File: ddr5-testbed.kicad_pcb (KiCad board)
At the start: 6 copper layers, 69.6 x 30 mm, 67 parts, among them IC1 PCA6408APW, IC2 AT24CS01, J1 ddr4-sodimm-edge-connector, U1 MT60B2G8HB-48B_A, U2 TPS613221ADBVT

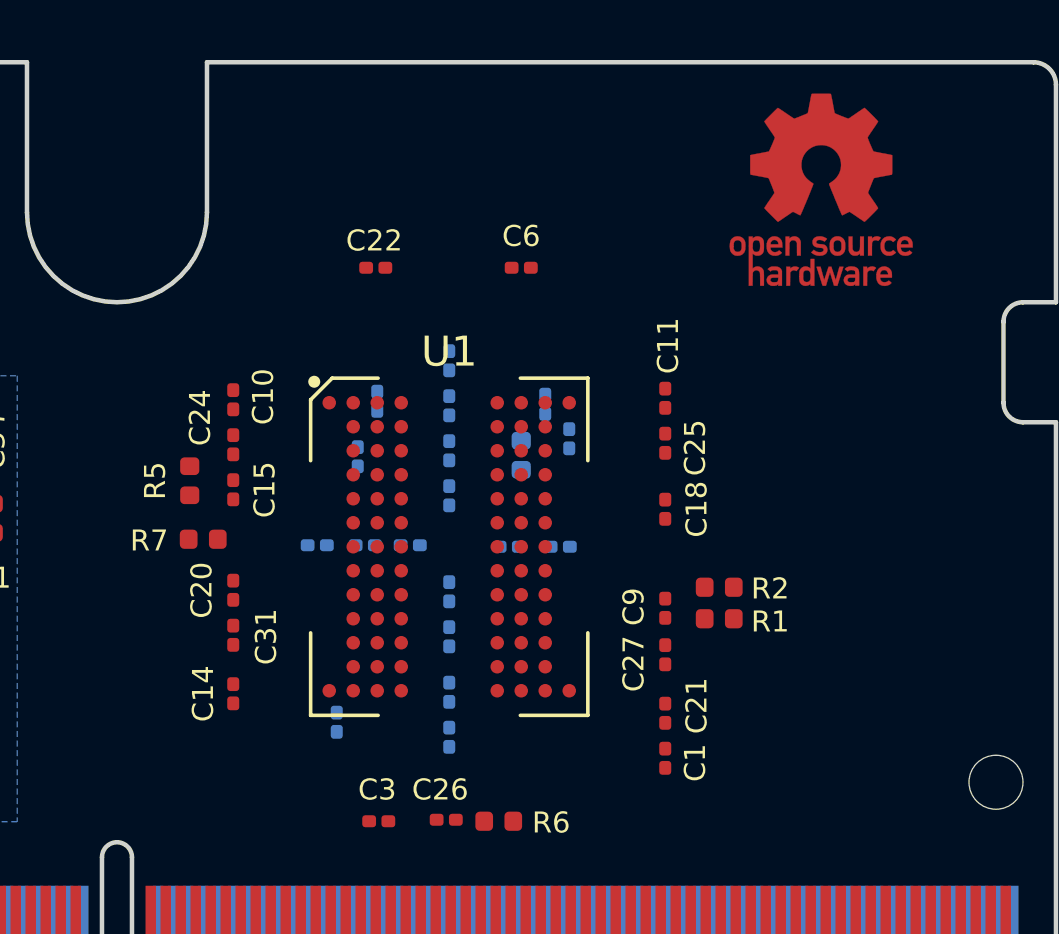
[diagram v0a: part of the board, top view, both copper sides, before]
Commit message: Fix power labels naming scheme, remove connection from SODIM to VDDQ, add chockes to DDR5 power
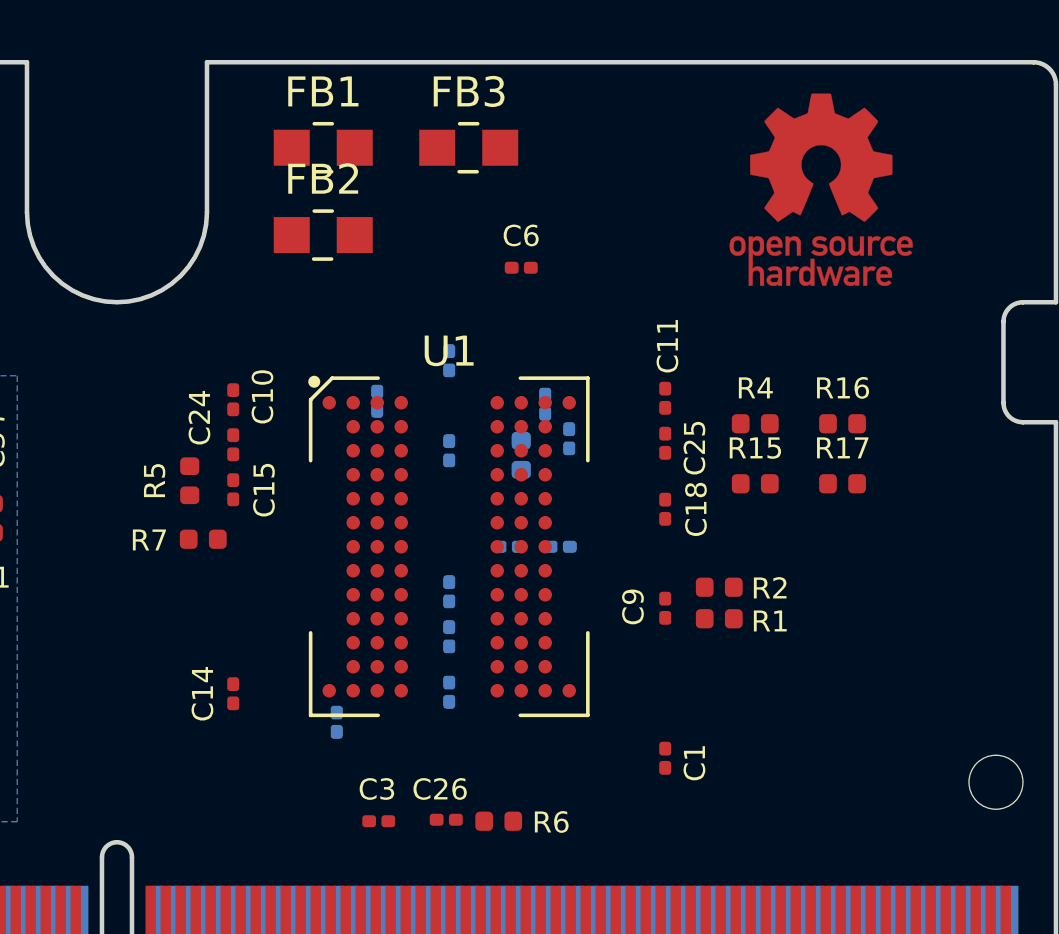
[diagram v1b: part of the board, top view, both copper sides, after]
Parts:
- removed C16, C17, C19, C20, C21, C22, C27, C29, C31, C33, C35, C36: C_100n_0201, ddr5-testbed-footprints:0201-res
- added FB1: 742792022, ddr5-testbed-footprints:0805-res, F.Cu at (145.2, 72.8)
- added FB2: 742792022, ddr5-testbed-footprints:0805-res, F.Cu at (145.2, 75.8)
- added FB3: 742792022, ddr5-testbed-footprints:0805-res, F.Cu at (150.0, 72.8)
- added R15: R_0R_0402, ddr5-testbed-footprints:0402-res, F.Cu at (159.6, 84.0)
- added R16: R_0R_0402, ddr5-testbed-footprints:0402-res, F.Cu at (162.5, 82.0)
- added R17: R_0R_0402, ddr5-testbed-footprints:0402-res, F.Cu at (162.5, 84.0)
- added R4: R_0R_0402, ddr5-testbed-footprints:0402-res, F.Cu at (159.6, 82.0)
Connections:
- net VDDLED renamed /EEPROM/VDD_LED
- C12 pad 1: VDD2 -> VDD
- C15 pad 1: VDD2 -> VDD
- C18 pad 1: VDD2 -> VDDQ
- C23 pad 1: VDD2 -> VDD
- C24 pad 1: VDD1 -> VPP
- C25 pad 1: VDD1 -> VPP
- C26 pad 1: VDD2 -> VDD
- C28 pad 1: VDD2 -> VDD
- C3 pad 1: VDD2 -> VDD
- C30 pad 1: VDD2 -> VDD
- C32 pad 1: VDD2 -> VDD
- C34 pad 1: VDD1 -> 1V8_SYS
- C38 pad 1: VDD1 -> 1V8_SYS
- C39 pad 1: VDD1 -> 1V8_SYS
- C6 pad 1: VDD2 -> VDD
- C9 pad 1: VDD2 -> VDD
- IC1 pad 1: VDD1 -> 1V8_SYS
- IC1 pad 2: VDD1 -> 1V8_SYS
- IC1 pad 3: VDD1 -> 1V8_SYS
- IC2 pad 4: VDD1 -> 1V8_SYS
- J1 pad 101: VDD2 -> 1V1_SYS
- J1 pad 103: VDD2 -> 1V1_SYS
- J1 pad 105: VDD2 -> 1V1_SYS
- J1 pad 107: VDD2 -> 1V1_SYS
- J1 pad 116: VDD1 -> 1V8_SYS
- J1 pad 118: VDD1 -> 1V8_SYS
- J1 pad 120: VDD1 -> 1V8_SYS
- J1 pad 122: VDD1 -> 1V8_SYS
- J1 pad 124: VDD1 -> 1V8_SYS
- J1 pad 126: VDDQ -> (no net)
- J1 pad 128: VDDQ -> (no net)
- J1 pad 130: VDDQ -> (no net)
- J1 pad 156: (no net) -> CA5
- J1 pad 158: (no net) -> CA4
- J1 pad 160: (no net) -> CA3
- J1 pad 162: (no net) -> CA2
- J1 pad 163: (no net) -> CA9
- J1 pad 164: (no net) -> CLK_N
- J1 pad 165: (no net) -> CA8
- J1 pad 166: (no net) -> CLK_P
- J1 pad 167: (no net) -> CA7
- J1 pad 169: (no net) -> CA6
- J1 pad 171: (no net) -> MIR
- J1 pad 172: (no net) -> ALERT_N
- J1 pad 173: (no net) -> TDQS_N
- J1 pad 174: (no net) -> LBDQ
- J1 pad 175: (no net) -> TDQS_P
- J1 pad 176: (no net) -> LBDQS
- J1 pad 179: (no net) -> CA13
- J1 pad 181: (no net) -> CA12
- J1 pad 183: (no net) -> CA11
- J1 pad 185: (no net) -> CA10
- J1 pad 187: (no net) -> DQ4
- J1 pad 189: (no net) -> DQ5
- J1 pad 191: (no net) -> DQ6
- J1 pad 193: (no net) -> DQ7
- J1 pad 194: (no net) -> CS_N
- J1 pad 196: (no net) -> TEN
- J1 pad 197: (no net) -> CAI
- J1 pad 199: (no net) -> DQS_N
- J1 pad 201: (no net) -> DQS_P
- J1 pad 203: (no net) -> DQ0
- J1 pad 204: (no net) -> CA0
- J1 pad 205: (no net) -> DQ1
- J1 pad 206: (no net) -> CA1
- J1 pad 207: (no net) -> DQ2
- J1 pad 209: (no net) -> DQ3
- J1 pad 246: VDDQ -> (no net)
- J1 pad 248: VDDQ -> (no net)
- J1 pad 250: VDDQ -> (no net)
- J1 pad 93: VDD2 -> 1V1_SYS
- J1 pad 95: VDD2 -> 1V1_SYS
- J1 pad 97: VDD2 -> 1V1_SYS
- J1 pad 99: VDD2 -> 1V1_SYS
- L1 pad 1: VDD1 -> 1V8_SYS
- R13 pad 1: VDD1 -> 1V8_SYS
- R14 pad 1: VDD1 -> 1V8_SYS
- R8 pad 1: VDD1 -> 1V8_SYS
- U1 pad A10: (no net) -> LBDQS
- U1 pad A2: (no net) -> LBDQ
- U1 pad A4: VDD2 -> VPP
- U1 pad B10: VDD1 -> VDD
- U1 pad B2: VDD1 -> VDD
- U1 pad B4: (no net) -> DQ2
- U1 pad B8: (no net) -> DQ3
- U1 pad C3: (no net) -> DQ0
- U1 pad C4: (no net) -> DQS_P
- U1 pad C8: (no net) -> TDQS_P
- U1 pad C9: (no net) -> DQ1
- U1 pad D4: (no net) -> DQS_N
- U1 pad D8: (no net) -> TDQS_N
- U1 pad E10: VDD1 -> VDD
- U1 pad E2: VDD1 -> VDD
- U1 pad E3: (no net) -> DQ4
- U1 pad E4: (no net) -> DQ6
- U1 pad E8: (no net) -> DQ7
- U1 pad E9: (no net) -> DQ5
- U1 pad G10: (no net) -> Net-(R17-Pad1)
- U1 pad G3: (no net) -> Net-(R16-Pad1)
- U1 pad G4: VDD1 -> VDD
- U1 pad G8: (no net) -> CLK_P
- U1 pad H10: VDD1 -> VDD
- U1 pad H2: (no net) -> Net-(R4-Pad1)
- U1 pad H8: (no net) -> CLK_N
- U1 pad J3: (no net) -> CA4
- U1 pad J4: (no net) -> CA0
- U1 pad J8: (no net) -> CA1
- U1 pad J9: (no net) -> CA5
- U1 pad K10: VDD1 -> VDD
- U1 pad K2: VDD1 -> VDD
- U1 pad K3: (no net) -> CA6
- U1 pad K4: (no net) -> CA2
- U1 pad K8: (no net) -> CA3
- U1 pad K9: (no net) -> CA7
- U1 pad L4: (no net) -> CA8
- U1 pad L8: (no net) -> CA9
- U1 pad M2: (no net) -> Net-(R15-Pad1)
- U1 pad M3: (no net) -> CA10
- U1 pad M4: (no net) -> CA12
- U1 pad M8: (no net) -> CA13
- U1 pad M9: (no net) -> CA11
- U1 pad N10: VDD1 -> VDD
- U1 pad N2: VDD1 -> VDD
- U1 pad N4: VDD1 -> VDD
- U1 pad N8: VDD2 -> VPP
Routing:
- net VDD1: track 21.9 -> 0.00 mm, vias 9 -> 0
- net 1V8_SYS: track 0.00 -> 21.9 mm, vias 0 -> 9
- added copper zone on B.Cu, net 1V8_SYS
- removed copper zone on B.Cu, net VDD1

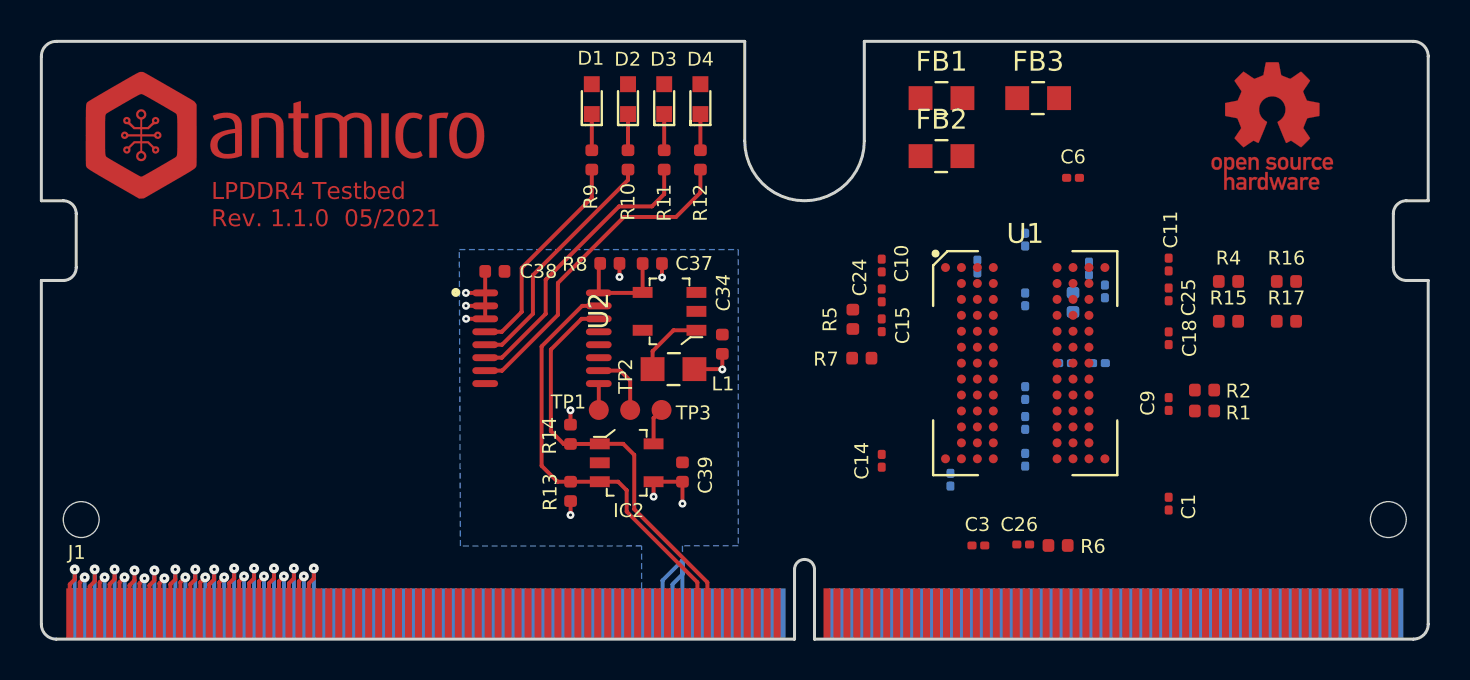
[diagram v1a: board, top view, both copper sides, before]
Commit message: Update silks default values, update project name on PCB
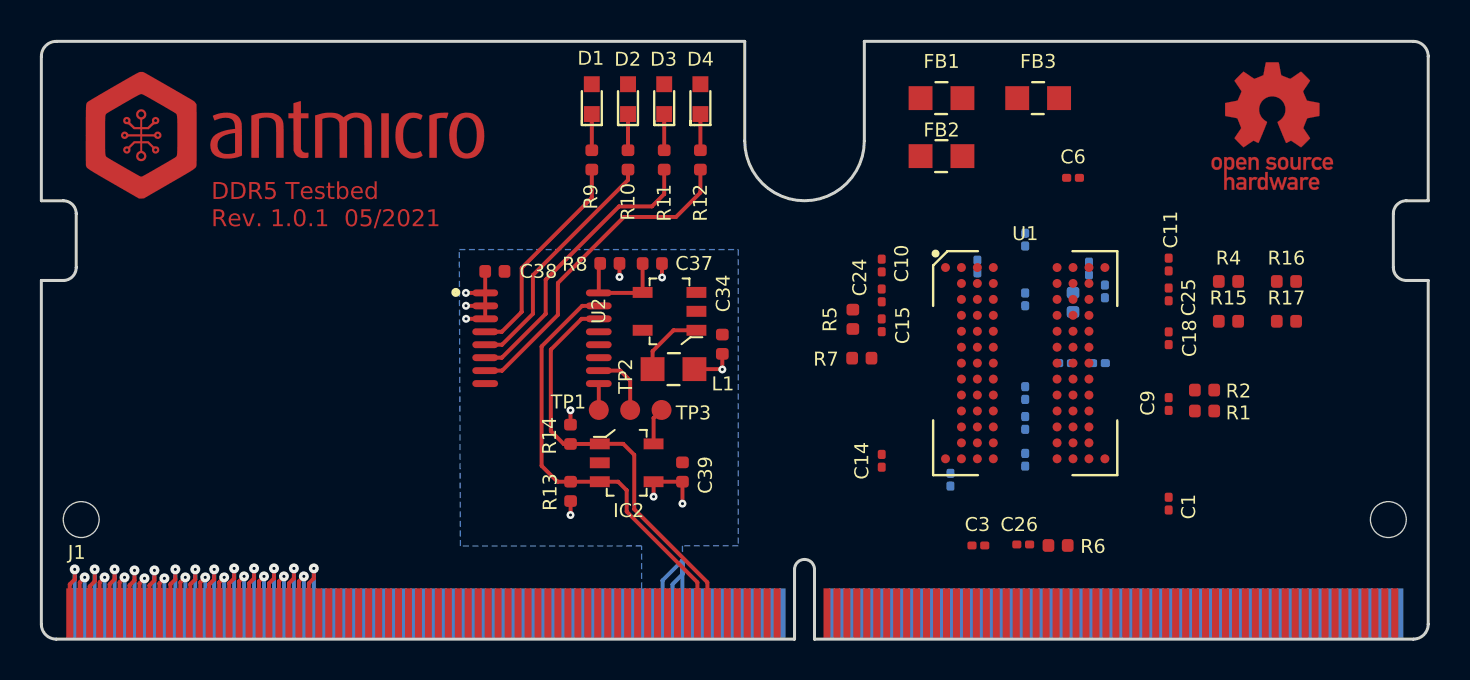
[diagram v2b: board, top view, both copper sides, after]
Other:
- board text added: "DDR5 Testbed Rev. 1.0.1 05/2021"
- board text removed: "LPDDR4 Testbed Rev. 1.1.0 05/2021"

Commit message: Update net classes to match impedance, import changes from sch, add dummy 3D model of DDR5 IC
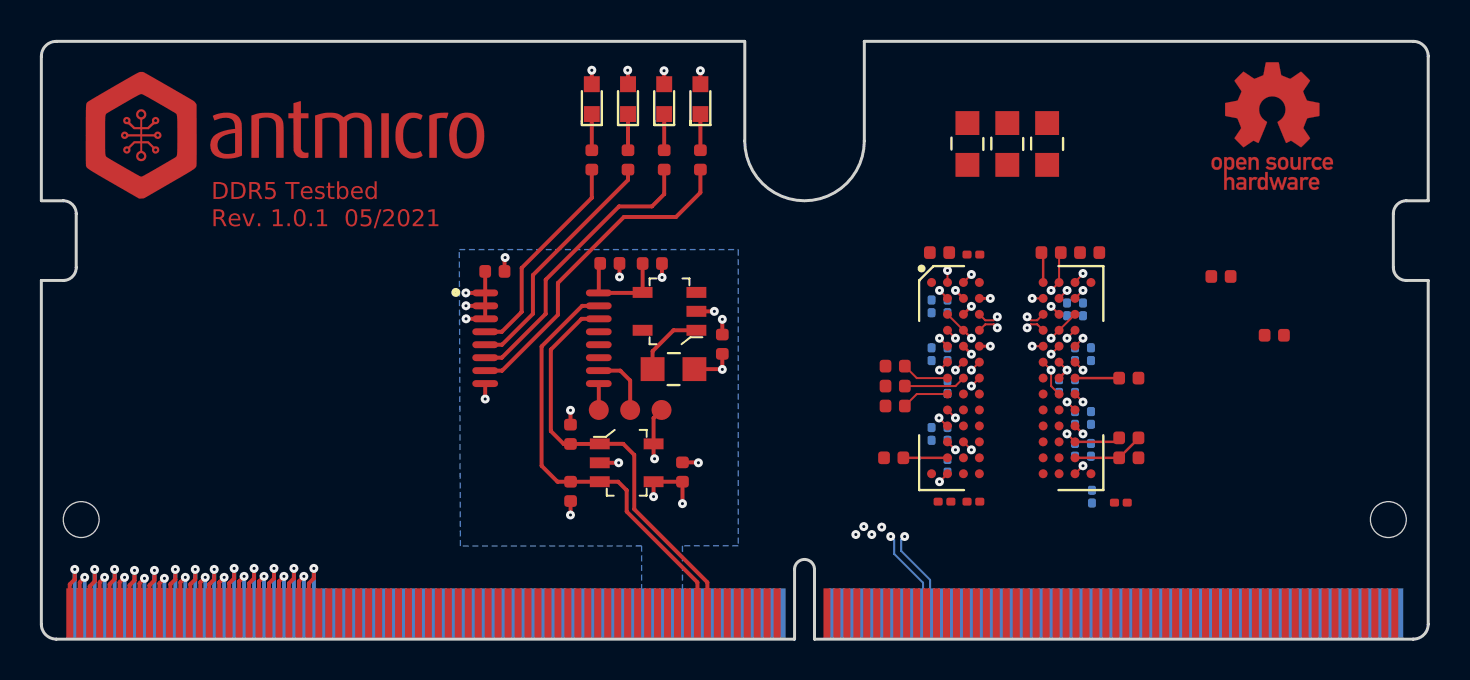
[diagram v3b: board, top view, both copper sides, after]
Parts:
- added R18: R_0R_0402, ddr5-testbed-footprints:0402-res, F.Cu at (145.1, 80.6)
- added R19: R_0R_0402, ddr5-testbed-footprints:0402-res, F.Cu at (152.6, 80.6)
- C1, C10, C11, C14, C15, C18, C3, C9: moved to B.Cu
- R3: moved to F.Cu
- moved R16 20.3 mm to (142.8, 87.3), turned to 180 degrees
- moved R15 18.1 mm to (142.8, 90.9), turned to 180 degrees
- moved R4 17.9 mm to (142.8, 88.3), turned to 180 degrees
- moved C6 17.5 mm to (145.3, 93.1)
- moved C24 15.9 mm to (154.2, 93.2), turned to 0 degrees
- moved R2 15.6 mm to (142.8, 86.3), turned to 180 degrees
- moved R5 15.1 mm to (154.6, 89.9), turned to 0 degrees
- moved R6 14.7 mm to (150.7, 80.6)
- moved R7 14.3 mm to (154.6, 90.9)
- moved C15 13.6 mm to (152.7, 92.8)
- moved C1 12.5 mm to (145.5, 87.3), turned to 270 degrees
- moved C9 12.2 mm to (144.7, 85.7), turned to 270 degrees
- moved C18 12.1 mm to (145.5, 89.7)
- moved C11 12.0 mm to (145.5, 85.7), turned to 270 degrees
- moved C10 10.6 mm to (145.5, 91.3)
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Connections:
- J1 pad 156: CA5 -> DQ4
- J1 pad 158: CA4 -> DQ6
- J1 pad 160: CA3 -> DQ0
- J1 pad 162: CA2 -> DQ2
- J1 pad 163: CA9 -> CA10
- J1 pad 164: CLK_N -> DQS_N
- J1 pad 165: CA8 -> CA12
- J1 pad 166: CLK_P -> DQS_P
- J1 pad 167: CA7 -> CA8
- J1 pad 170: (no net) -> DQ3
- J1 pad 171: MIR -> CA2
- J1 pad 172: ALERT_N -> DQ1
- J1 pad 173: TDQS_N -> CLK_N
- J1 pad 174: LBDQ -> DQ7
- J1 pad 175: TDQS_P -> CLK_P
- J1 pad 176: LBDQS -> DQ5
- J1 pad 179: CA13 -> CA0
- J1 pad 181: CA12 -> CA4
- J1 pad 183: CA11 -> CA13
- J1 pad 185: CA10 -> CA11
- J1 pad 187: DQ4 -> CA9
- J1 pad 189: DQ5 -> CA3
- J1 pad 191: DQ6 -> CA7
- J1 pad 192: OTD_CA_A -> (no net)
- J1 pad 193: DQ7 -> CA1
- J1 pad 194: CS_N -> (no net)
- J1 pad 196: TEN -> TDQS_P
- J1 pad 197: CAI -> CA5
- J1 pad 198: (no net) -> TDQS_N
- J1 pad 199: DQS_N -> (no net)
- J1 pad 201: DQS_P -> (no net)
- J1 pad 203: DQ0 -> (no net)
- J1 pad 204: CA0 -> LBDQ
- J1 pad 205: DQ1 -> (no net)
- J1 pad 206: CA1 -> LBDQS
- J1 pad 207: DQ2 -> (no net)
- J1 pad 209: DQ3 -> (no net)
- R15 pad 2: CAI -> (no net)
- R16 pad 2: MIR -> (no net)
- R17 pad 2: TEN -> (no net)
- R2 pad 2: OTD_CA_A -> (no net)
- R4 pad 2: ALERT_N -> (no net)
- U1 pad A10: LBDQS -> Net-(R19-Pad1)
- U1 pad A2: LBDQ -> Net-(R18-Pad1)
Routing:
- net DQS_P: track 0.00 -> 20.6 mm, vias 0 -> 2
- net DQS_N: track 0.00 -> 20.0 mm, vias 0 -> 2
- net DQ1: track 0.00 -> 19.2 mm, vias 0 -> 1
- net GND: track 105.6 -> 124.5 mm, vias 26 -> 46
- net DQ7: track 0.00 -> 16.0 mm, vias 0 -> 1
- net DQ5: track 0.00 -> 15.8 mm, vias 0 -> 1
- net DQ6: track 0.00 -> 13.5 mm, vias 0 -> 2
- net DQ4: track 0.00 -> 11.9 mm, vias 0 -> 2
- net DQ3: track 0.00 -> 9.23 mm, vias 0 -> 1
- net 1V8_SYS: track 21.9 -> 13.4 mm
- net VDDQ: track 0.00 -> 8.52 mm, vias 0 -> 10
- net DQ2: track 0.00 -> 6.32 mm, vias 0 -> 2
- net VDD: track 0.00 -> 5.68 mm, vias 0 -> 10
- net DQ0: track 0.00 -> 5.05 mm, vias 0 -> 2
- net Net-(R5-Pad2): track 0.00 -> 3.62 mm
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- added copper zone on In3.Cu, net GND
- added copper zone on In2.Cu, net VDD
- added copper zone on In2.Cu, net VDDQ
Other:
- net class Default: clearance 0.1 -> 0.1016; trace_width 0.1 -> 0.1016; via_dia 0.4 -> 0.45
- net class SE50_inner added: clearance 0.1016, trace_width 0.1016, via_dia 0.45, via_drill 0.15
- net class SE50_outer added: clearance 0.1016, trace_width 0.145, via_dia 0.45, via_drill 0.15
- net class Z100_inner added: clearance 0.1016, trace_width 0.1016, via_dia 0.45, via_drill 0.15
- net class Z100_outer added: clearance 0.1016, trace_width 0.1016, via_dia 0.45, via_drill 0.15
- rule trace_clearance: 0.1 -> 0.1016

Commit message: Remap connections
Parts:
- C26, C6: moved to B.Cu
- moved FB3 18.7 mm to (138.2, 89.2), turned to 0 degrees
- moved FB1 14.6 mm to (138.2, 87.2), turned to 0 degrees
- moved FB2 14.4 mm to (138.2, 85.2), turned to 0 degrees
- moved R3 14.1 mm to (148.8, 79.4), turned to 90 degrees
- moved R18 12.5 mm to (157.5, 81.7), turned to 90 degrees
- moved R15 12.4 mm to (147.2, 79.3), turned to 90 degrees
- moved C3 11.9 mm to (156.5, 88.8), turned to 0 degrees
- moved R2 11.3 mm to (151.8, 79.4), turned to 90 degrees
- moved R4 11.3 mm to (149.8, 79.4), turned to 90 degrees
- moved R16 11.2 mm to (150.8, 79.4), turned to 90 degrees
- moved C18 11.1 mm to (156.5, 88.0), turned to 0 degrees
- moved C6 11.0 mm to (145.3, 82.1), turned to 270 degrees
- moved C25 11.0 mm to (157.4, 83.3), turned to 90 degrees
- moved C24 10.9 mm to (145.0, 87.2), turned to 270 degrees
- moved C30 10.9 mm to (155.2, 80.4), turned to 90 degrees
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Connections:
- J1 pad 156: DQ4 -> (no net)
- J1 pad 158: DQ6 -> (no net)
- J1 pad 160: DQ0 -> (no net)
- J1 pad 162: DQ2 -> (no net)
- J1 pad 163: CA10 -> CA12
- J1 pad 164: DQS_N -> CAI
- J1 pad 165: CA12 -> CA10
- J1 pad 166: DQS_P -> ALERT_N
- J1 pad 170: DQ3 -> (no net)
- J1 pad 172: DQ1 -> MIR
- J1 pad 174: DQ7 -> OTD_CA_A
- J1 pad 176: DQ5 -> CS_N
- J1 pad 178: (no net) -> DQ5
- J1 pad 179: CA0 -> CA4
- J1 pad 180: (no net) -> DQ7
- J1 pad 181: CA4 -> CA0
- J1 pad 182: (no net) -> DQ1
- J1 pad 183: CA13 -> CA11
- J1 pad 185: CA11 -> CA13
- J1 pad 186: RESET_N -> DQ3
- J1 pad 189: CA3 -> CA7
- J1 pad 191: CA7 -> CA3
- J1 pad 192: (no net) -> DQ4
- J1 pad 193: CA1 -> CA5
- J1 pad 194: (no net) -> DQ6
- J1 pad 196: TDQS_P -> DQS_N
- J1 pad 197: CA5 -> CA1
- J1 pad 198: TDQS_N -> DQS_P
- J1 pad 199: (no net) -> TDQS_N
- J1 pad 201: (no net) -> TDQS_P
- J1 pad 203: (no net) -> RESET_N
- J1 pad 204: LBDQ -> DQ2
- J1 pad 205: (no net) -> TEN
- J1 pad 206: LBDQS -> DQ0
- J1 pad 207: (no net) -> LBDQS
- J1 pad 209: (no net) -> LBDQ
- R15 pad 2: (no net) -> CAI
- R16 pad 2: (no net) -> MIR
- R17 pad 2: (no net) -> TEN
- R2 pad 2: (no net) -> OTD_CA_A
- R4 pad 2: (no net) -> ALERT_N
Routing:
- net OTD_CA_A: track 0.00 -> 30.6 mm, vias 0 -> 1
- net GND: track 124.5 -> 155.0 mm, vias 46 -> 56
- net MIR: track 0.00 -> 29.8 mm, vias 0 -> 1
- net CS_N: track 0.00 -> 28.6 mm, vias 0 -> 1
- net ALERT_N: track 0.00 -> 28.4 mm, vias 0 -> 1
- net CAI: track 0.00 -> 27.1 mm, vias 0 -> 1
- net VPP: track 0.00 -> 25.7 mm
- net LBDQ: track 0.00 -> 22.3 mm
- net CA4: track 0.00 -> 22.2 mm, vias 0 -> 2
- net CA0: track 0.00 -> 21.3 mm, vias 0 -> 2
- net CA8: track 0.00 -> 20.9 mm, vias 0 -> 2
- net CA6: track 0.00 -> 20.9 mm, vias 0 -> 2
- net CA10: track 0.00 -> 20.6 mm, vias 0 -> 2
- net CA2: track 0.00 -> 19.8 mm, vias 0 -> 2
- net CA12: track 0.00 -> 19.5 mm, vias 0 -> 2
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- added copper zone on F.Cu, net 1V1_SYS
- added copper zone on In4.Cu, net 1V1_SYS
- added copper zone on F.Cu, net VDD
- added copper zone on In4.Cu, net VDD
- added copper zone on F.Cu, net VDDQ
- added copper zone on In1.Cu, net VDDQ
- removed copper zone on In2.Cu, net VDD
- removed copper zone on In2.Cu, net VDDQ
